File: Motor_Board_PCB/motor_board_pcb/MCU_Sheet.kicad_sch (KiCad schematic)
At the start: 63 parts, among them J1 CX90B-16P, J2 Barrel_Jack_Switch, J3 TSM-105-01-S-DV-M-TR, J5 PH2-06-UA, SW2 SW_Push, U1 R7FA4M1AB3CFM, U2 AP63205WU-7, Y1 16MHz?

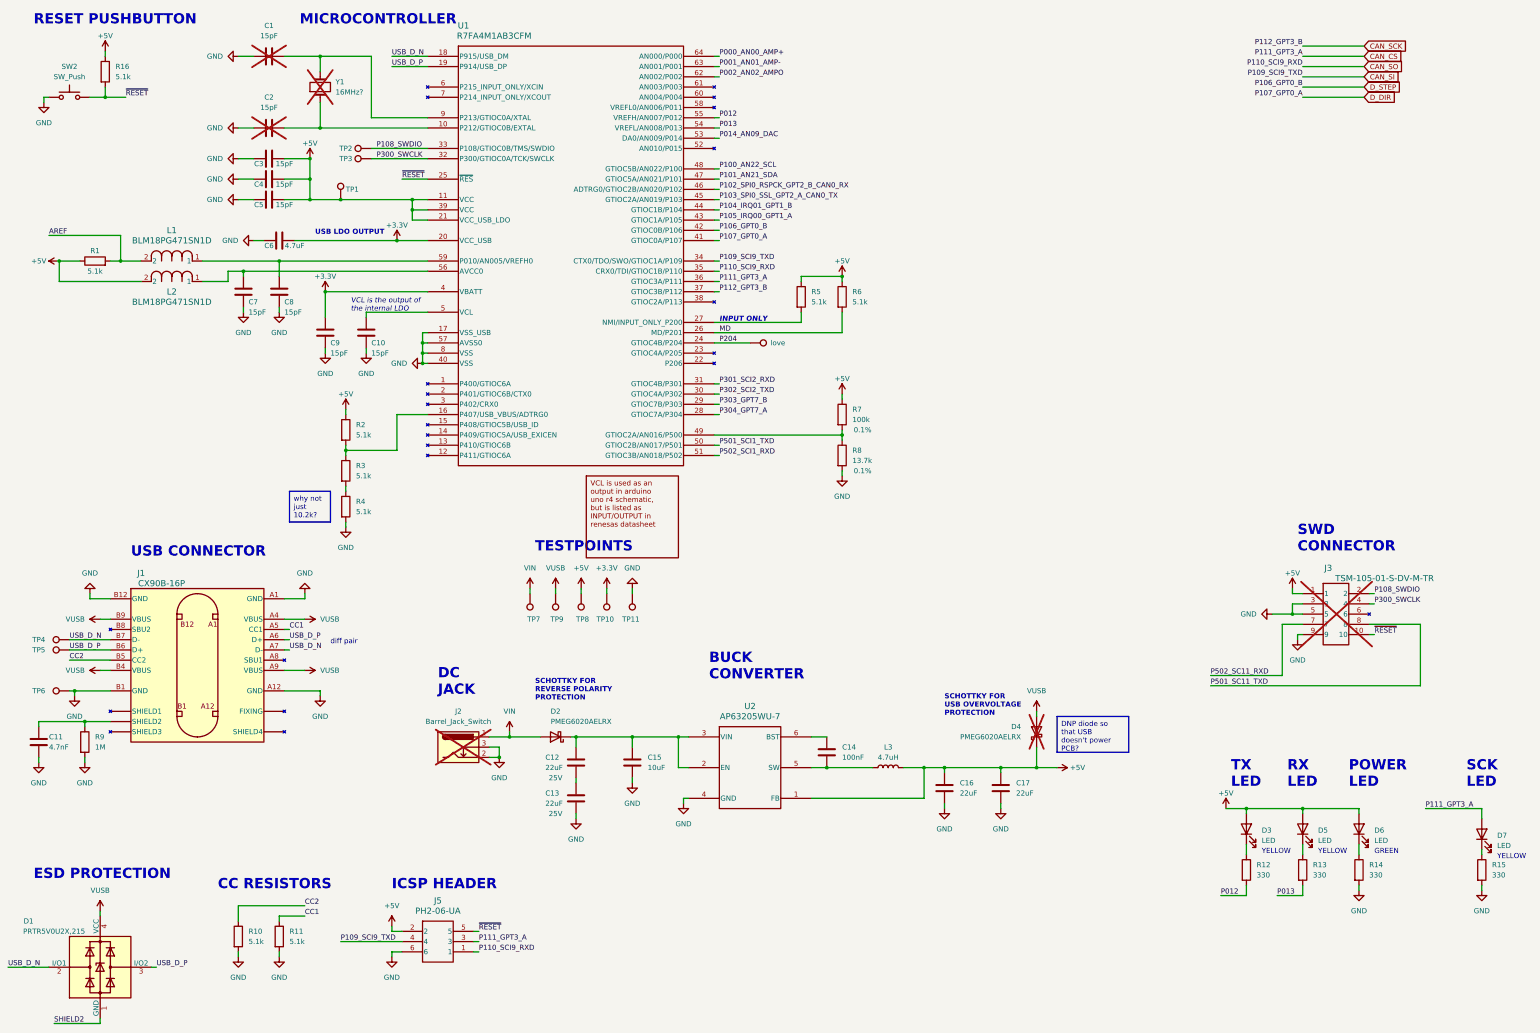
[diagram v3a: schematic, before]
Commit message: Added footprints for almost all components
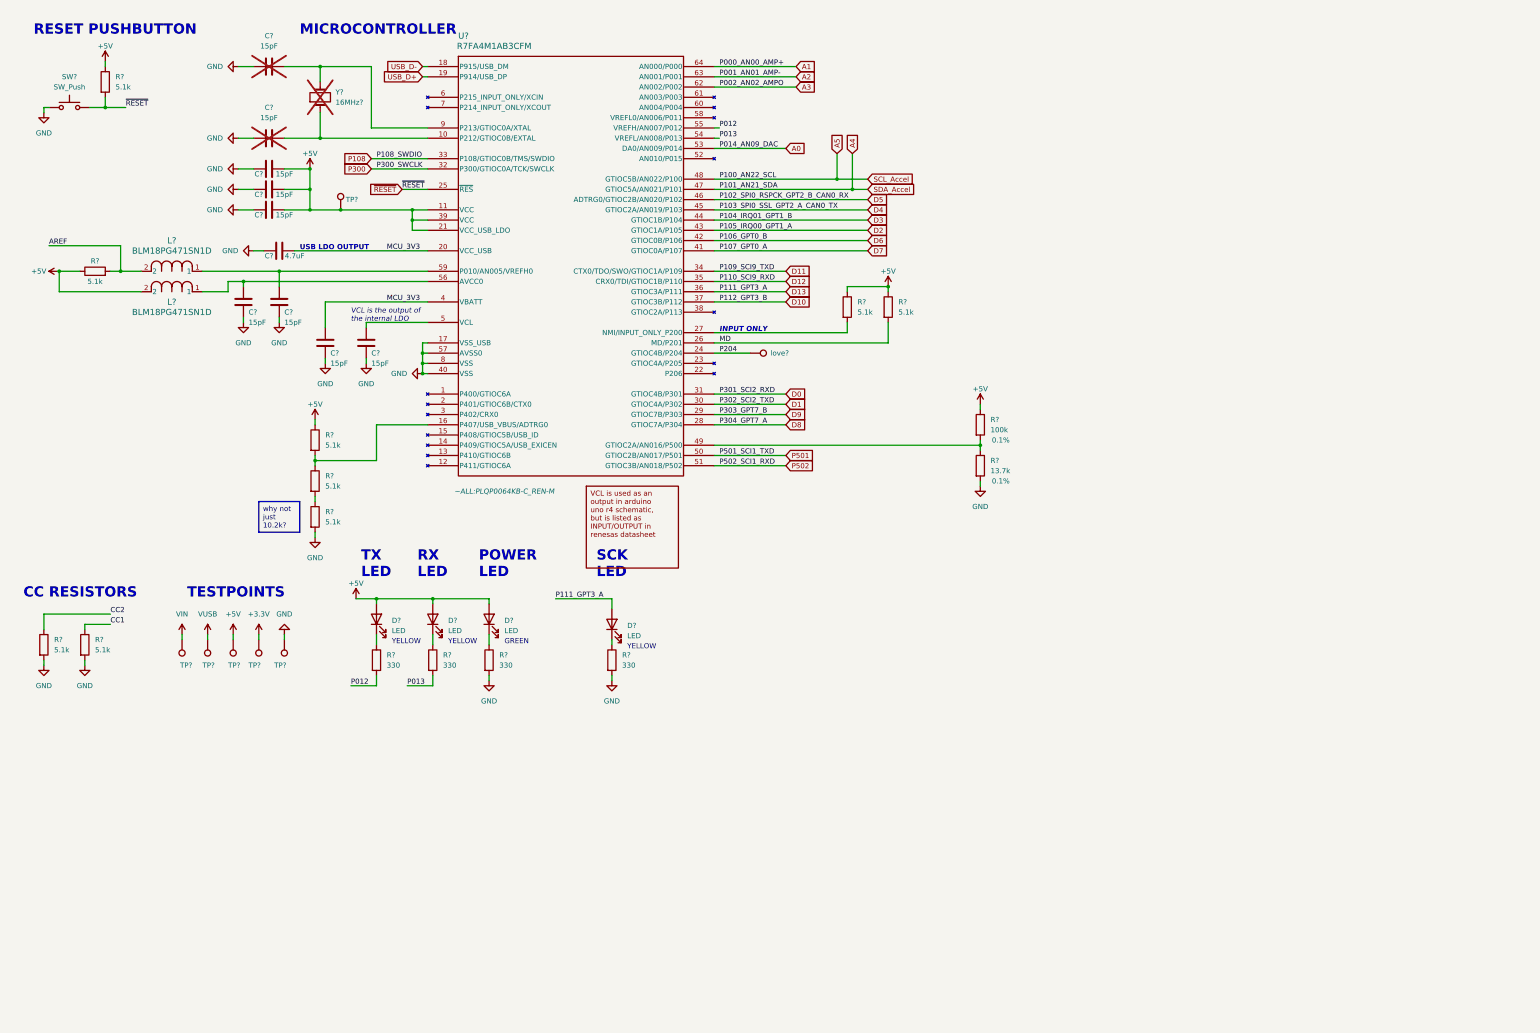
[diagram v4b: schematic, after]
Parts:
- removed C1, C10, C2, C3, C4, C5, C7, C8, C9: 15pF, symbol Device:C
- removed C11: 4.7nF, symbol Device:C
- removed C12, C13, C16, C17: 22uF, symbol Device:C
- removed C14: 100nF, symbol Device:C
- removed C15: 10uF, symbol Device:C
- removed C6: 4.7uF, symbol Device:C
- removed D1: PRTR5V0U2X,215, Package_TO_SOT_SMD:SOT-143, symbol Power_Protection:PRTR5V0U2X
- removed D2, D4: PMEG6020AELRX, Diode_SMD:Nexperia_CFP3_SOD-123W, symbol Diode:PMEG6020AELR
- removed D3, D5, D6, D7: LED, symbol Device:LED
- removed J1: CX90B-16P, CON18_1X12_P0_HIR, symbol CX90B-16P:CX90B-16P
- removed J2: Barrel_Jack_Switch, symbol Connector:Barrel_Jack_Switch
- removed J3: TSM-105-01-S-DV-M-TR, CONN_TSM-105-01-S-DV-M-TR_SAI, symbol TSM-105-01-S-DV-M-TR:TSM-105-01-S-DV-M-TR
- removed J5: PH2-06-UA, CONN_PH2-06-UA_ADM, symbol PH2-06-UA:PH2-06-UA
- removed L1, L2: BLM18PG471SN1D, IND_BLM18_0603_MUR, symbol BLM18PG471SN1D:BLM18PG471SN1D
- removed L3: 4.7uH, symbol Device:L
- removed R1, R10, R11, R16, R2, R3, R4, R5, R6: 5.1k, symbol Device:R
- removed R12, R13, R14, R15: 330, symbol Device:R
- removed R7: 100k, symbol Device:R
- removed R8: 13.7k, symbol Device:R
- removed R9: 1M, symbol Device:R
- removed SW2: SW_Push, symbol Switch:SW_Push
- removed TP1, TP10, TP11, TP2, TP3, TP4, TP5, TP6, TP7, TP8, TP9, love: TestPoint, symbol Connector:TestPoint
- removed U1: R7FA4M1AB3CFM, PLQP0064KB-C_REN, symbol R7FA4M1AB3CFM:R7FA4M1AB3CFM
- removed U2: AP63205WU-7, SOIC_05WU-7_DIO, symbol AP63205WU-7:AP63205WU-7
- removed Y1: 16MHz?, symbol Device:Crystal
- added C? (x9): 15pF, Capacitor_SMD:C_0603_1608Metric, symbol Device:C
- added C?: 4.7uF, Capacitor_SMD:C_0603_1608Metric, symbol Device:C
- added D? (x4): LED, Diode_SMD:D_0603_1608Metric, symbol Device:LED
- added L? (x2): BLM18PG471SN1D, ~ALL:IND_BLM18_0603_MUR, symbol BLM18PG471SN1D:BLM18PG471SN1D
- added R? (x4): 330, Resistor_SMD:R_0603_1608Metric, symbol Device:R
- added R? (x9): 5.1k, Resistor_SMD:R_0603_1608Metric, symbol Device:R
- added R?: 13.7k, Resistor_SMD:R_0603_1608Metric, symbol Device:R
- added R?: 100k, Resistor_SMD:R_0603_1608Metric, symbol Device:R
- added SW?: SW_Push, Button_Switch_SMD:SW_Push_1P1T_NO_6x6mm_H9.5mm, symbol Switch:SW_Push
- added TP? (x6): TestPoint, TestPoint:TestPoint_Pad_D1.0mm, symbol Connector:TestPoint
- added U?: R7FA4M1AB3CFM, ~ALL:PLQP0064KB-C_REN-M, symbol R7FA4M1AB3CFM:R7FA4M1AB3CFM
- added Y?: 16MHz?, symbol Device:Crystal
- added love?: TestPoint, TestPoint:TestPoint_Pad_D2.0mm, symbol Connector:TestPoint
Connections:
- net +3.3V: now also TP?.1
- net +5V: now also C?.2, C?.2, C?.2, D?.2 (A), D?.2 (A), D?.2 (A), L?.2, R?.1, R?.1, R?.1, R?.1, R?.1, R?.1, TP?.1, TP?.1, U?.11 (VCC), U?.21 (VCC_USB_LDO), U?.39 (VCC)
- net AREF: now also L?.2, R?.2
- net CC1: now also R?.1
- net CC2: now also R?.1
- net GND: now also C?.1, C?.1, C?.1, C?.1, C?.1, C?.1, C?.1, C?.1, C?.1, C?.1, R?.2, R?.2, R?.2, R?.2, R?.2, R?.2, SW?.1, TP?.1, U?.17 (VSS_USB), U?.40 (VSS), U?.57 (AVSS0), U?.8 (VSS)
- net MD: now also R?.2, U?.26 (MD/P201)
- net P012: now also R?.2, U?.55 (VREFH/AN007/P012)
- net P013: now also R?.2, U?.54 (VREFL/AN008/P013)
- net P204: now also U?.24 (GTIOC4B/P204), love?.1
- net VUSB: now also TP?.1, TP?.1
- net ~{RESET}: now also R?.2, SW?.2, U?.25 (~{RES})
- new net: D?.1 (K), R?.1 (x4)
- new net: C?.2, U?.9 (P213/GTIOC0A/XTAL), Y?.2
- new net: C?.2, L?.1, U?.59 (P010/AN005/VREFH0)
- new net: R?.1, R?.2, U?.16 (P407/USB_VBUS/ADTRG0)
- new net: R?.1, R?.2
- new net: C?.2, U?.10 (P212/GTIOC0B/EXTAL), Y?.1
- new net: R?.2, U?.27 (NMI/INPUT_ONLY_P200)
- new net: R?.1, R?.2, U?.49 (GTIOC2A/AN016/P500)
- new net: C?.2, U?.5 (VCL)
- new net: C?.2, L?.1, U?.56 (AVCC0)
- new net A0: U?.53 (DA0/AN009/P014)
- new net A1: U?.64 (AN000/P000)
- new net A2: U?.63 (AN001/P001)
- new net A3: U?.62 (AN002/P002)
- new net A4: U?.47 (GTIOC5A/AN021/P101)
- new net A5: U?.48 (GTIOC5B/AN022/P100)
- new net D0: U?.31 (GTIOC4B/P301)
- new net D1: U?.30 (GTIOC4A/P302)
- new net D10: U?.37 (GTIOC3B/P112)
- new net D11: U?.34 (CTX0/TDO/SWO/GTIOC1A/P109)
- new net D12: U?.35 (CRX0/TDI/GTIOC1B/P110)
- new net D13: D?.2 (A), U?.36 (GTIOC3A/P111)
- new net D2: U?.43 (GTIOC1A/P105)
- new net D3: U?.44 (GTIOC1B/P104)
- new net D4: U?.45 (GTIOC2A/AN019/P103)
- new net D5: U?.46 (ADTRG0/GTIOC2B/AN020/P102)
- new net D6: U?.42 (GTIOC0B/P106)
- new net D7: U?.41 (GTIOC0A/P107)
- new net D8: U?.28 (GTIOC7A/P304)
- new net D9: U?.29 (GTIOC7B/P303)
- new net MCU_3V3: C?.2, C?.2, U?.20 (VCC_USB), U?.4 (VBATT)
- new net P108: U?.33 (P108/GTIOC0B/TMS/SWDIO)
- new net P300: U?.32 (P300/GTIOC0A/TCK/SWCLK)
- new net P501: U?.50 (GTIOC2B/AN017/P501)
- new net P502: U?.51 (GTIOC3B/AN018/P502)
- new net USB_D+: U?.19 (P914/USB_DP)
- new net USB_D-: U?.18 (P915/USB_DM)
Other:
- note removed: "BUCK CONVERTER"
- note removed: "DC JACK"
- note removed: "ESD PROTECTION"
- note removed: "ICSP HEADER"
- note removed: "SCHOTTKY FOR REVERSE POLARITY PROTECTION"
- note removed: "SCHOTTKY FOR USB OVERVOLTAGE PROTECTION"
- note removed: "SWD CONNECTOR"
- note removed: "USB CONNECTOR"
- note removed: "diff pair"

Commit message: Added all other footprints... populated all components with NO errors or warnings :)
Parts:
- Y?: footprint (none) -> Crystal:Crystal_HC49-U_Vertical
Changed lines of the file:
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@@
       (effects (font (size 1.27 1.27)) (justify right))
     )
-    (property "Footprint" "" (at 92.71 41.91 0)
+    (property "Footprint" "Crystal:Crystal_HC49-U_Vertical" (at 92.71 41.91 0)
       (effects (font (size 1.27 1.27)) hide)
     )

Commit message: Meeting Changes
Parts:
- C? (x2), Y?: now fitted
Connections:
- net MD renamed BOOT
- net P108: no longer names the net of U?.33 (P108/GTIOC0B/TMS/SWDIO)
- net P300: no longer names the net of U?.32 (P300/GTIOC0A/TCK/SWCLK)
- net P501: no longer names the net of U?.50 (GTIOC2B/AN017/P501)
- net P502: no longer names the net of U?.51 (GTIOC3B/AN018/P502)
- no-connect marks 0 -> 4
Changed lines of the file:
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@@
   (junction (at 90.17 64.77) (diameter 0) (color 0 0 0 0)
   )
+  (junction (at 233.68 102.87) (diameter 0) (color 0 0 0 0)
+  )
   (junction (at 27.94 85.09) (diameter 0) (color 0 0 0 0)
   )
@@
   (junction (at 256.54 128.27) (diameter 0) (color 0 0 0 0)
   )
+  (no_connect (at 190.5 133.35))
+  (no_connect (at 119.38 59.69))
+  (no_connect (at 190.5 130.81))
+  (no_connect (at 119.38 57.15))
   (wire (pts (xy 190.5 54.61) (xy 208.28 54.61))
     (stroke (width 0) (type default))
@@
     (stroke (width 0) (type default))
   )
-  (wire (pts (xy 105.41 59.69) (xy 119.38 59.69))
-    (stroke (width 0) (type default))
-  )
   (wire (pts (xy 91.44 133.35) (xy 91.44 132.08))
     (stroke (width 0) (type default))
@@
     (stroke (width 0) (type default))
   )
-  (wire (pts (xy 190.5 133.35) (xy 208.28 133.35))
-    (stroke (width 0) (type default))
-  )
   (wire (pts (xy 40.64 85.09) (xy 43.18 85.09))
     (stroke (width 0) (type default))
@@
     (stroke (width 0) (type default))
   )
-  (wire (pts (xy 190.5 130.81) (xy 208.28 130.81))
-    (stroke (width 0) (type default))
-  )
   (wire (pts (xy 90.17 64.77) (xy 90.17 69.85))
     (stroke (width 0) (type default))
@@
     (stroke (width 0) (type default))
   )
+  (wire (pts (xy 233.68 102.87) (xy 237.49 102.87))
+    (stroke (width 0) (type default))
+  )
   (wire (pts (xy 190.5 128.27) (xy 256.54 128.27))
     (stroke (width 0) (type default))
@@
   )
   (wire (pts (xy 73.66 96.52) (xy 73.66 97.79))
-    (stroke (width 0) (type default))
-  )
-  (wire (pts (xy 105.41 57.15) (xy 119.38 57.15))
     (stroke (width 0) (type default))
   )
@@
     (effects (font (size 1.27 1.27)) (justify left bottom))
   )
-  (label "P502_SCI1_RXD" (at 191.77 133.35 0) (fields_autoplaced)
-    (effects (font (size 1.27 1.27)) (justify left bottom))
-  )
-  (label "CC1" (at 40.64 172.72 0) (fields_autoplaced)
-    (effects (font (size 1.27 1.27)) (justify left bottom))
-  )
   (label "~{RESET}" (at 113.03 64.77 0) (fields_autoplaced)
     (effects (font (size 1.27 1.27)) (justify left bottom))
@@
     (effects (font (size 1.27 1.27)) (justify left bottom))
   )
-  (label "P108_SWDIO" (at 106.68 57.15 0) (fields_autoplaced)
-    (effects (font (size 1.27 1.27)) (justify left bottom))
-  )
   (label "MD" (at 191.77 102.87 0) (fields_autoplaced)
     (effects (font (size 1.27 1.27)) (justify left bottom))
@@
     (effects (font (size 1.27 1.27)) (justify left bottom))
   )
-  (label "P501_SCI1_TXD" (at 191.77 130.81 0) (fields_autoplaced)
-    (effects (font (size 1.27 1.27)) (justify left bottom))
-  )
   (label "P110_SCI9_RXD" (at 191.77 87.63 0) (fields_autoplaced)
     (effects (font (size 1.27 1.27)) (justify left bottom))
@@
     (effects (font (size 1.27 1.27)) (justify left bottom))
   )
-  (label "CC2" (at 40.64 170.18 0) (fields_autoplaced)
-    (effects (font (size 1.27 1.27)) (justify left bottom))
-  )
   (label "P001_AN01_AMP-" (at 191.77 36.83 0) (fields_autoplaced)
     (effects (font (size 1.27 1.27)) (justify left bottom))
@@
     (effects (font (size 1.27 1.27)) (justify left bottom))
   )
-  (label "P300_SWCLK" (at 106.68 59.69 0) (fields_autoplaced)
-    (effects (font (size 1.27 1.27)) (justify left bottom))
+  (global_label "CC1" (shape input) (at 40.64 172.72 0) (fields_autoplaced)
+    (effects (font (size 1.27 1.27)) (justify left))
+    (property "Intersheetrefs" "${INTERSHEET_REFS}" (at 47.3747 172.72 0)
+      (effects (font (size 1.27 1.27)) (justify left) hide)
+    )
   )
   (global_label "USB_D+" (shape input) (at 118.11 36.83 180) (fields_autoplaced)
@@
     )
   )
+  (global_label "BOOT" (shape input) (at 237.49 102.87 0) (fields_autoplaced)
+    (effects (font (size 1.27 1.27)) (justify left))
+    (property "Intersheetrefs" "${INTERSHEET_REFS}" (at 245.3738 102.87 0)
+      (effects (font (size 1.27 1.27)) (justify left) hide)
+    )
+  )
   (global_label "SDA_Accel" (shape input) (at 228.6 64.77 0) (fields_autoplaced)
     (effects (font (size 1.27 1.27)) (justify left))
@@
     (property "Intersheetrefs" "${INTERSHEET_REFS}" (at 216.1033 36.83 0)
       (effects (font (size 1.27 1.27)) (justify left) hide)
-    )
-  )
-  (global_label "P108" (shape input) (at 105.41 57.15 180) (fields_autoplaced)
-    (effects (font (size 1.27 1.27)) (justify right))
-    (property "Intersheetrefs" "${INTERSHEET_REFS}" (at 97.5263 57.15 0)
-      (effects (font (size 1.27 1.27)) (justify right) hide)
     )
   )
@@
     )
   )
+  (global_label "CC2" (shape input) (at 40.64 170.18 0) (fields_autoplaced)
+    (effects (font (size 1.27 1.27)) (justify left))
+    (property "Intersheetrefs" "${INTERSHEET_REFS}" (at 47.3747 170.18 0)
+      (effects (font (size 1.27 1.27)) (justify left) hide)
+    )
+  )
   (global_label "D3" (shape input) (at 228.6 72.39 0) (fields_autoplaced)
     (effects (font (size 1.27 1.27)) (justify left))
@@
     )
   )
-  (global_label "P501" (shape input) (at 208.28 130.81 0) (fields_autoplaced)
-    (effects (font (size 1.27 1.27)) (justify left))
-    (property "Intersheetrefs" "${INTERSHEET_REFS}" (at 216.1637 130.81 0)
-      (effects (font (size 1.27 1.27)) (justify left) hide)
-    )
-  )
   (global_label "D1" (shape input) (at 208.28 118.11 0) (fields_autoplaced)
     (effects (font (size 1.27 1.27)) (justify left))
@@
     )
   )
-  (global_label "P300" (shape input) (at 105.41 59.69 180) (fields_autoplaced)
-    (effects (font (size 1.27 1.27)) (justify right))
-    (property "Intersheetrefs" "${INTERSHEET_REFS}" (at 97.5263 59.69 0)
-      (effects (font (size 1.27 1.27)) (justify right) hide)
-    )
-  )
   (global_label "A3" (shape input) (at 210.82 39.37 0) (fields_autoplaced)
     (effects (font (size 1.27 1.27)) (justify left))
@@
     (effects (font (size 1.27 1.27)) (justify left))
     (property "Intersheetrefs" "${INTERSHEET_REFS}" (at 216.1033 34.29 0)
-      (effects (font (size 1.27 1.27)) (justify left) hide)
-    )
-  )
-  (global_label "P502" (shape input) (at 208.28 133.35 0) (fields_autoplaced)
-    (effects (font (size 1.27 1.27)) (justify left))
-    (property "Intersheetrefs" "${INTERSHEET_REFS}" (at 216.1637 133.35 0)
       (effects (font (size 1.27 1.27)) (justify left) hide)
     )
@@
   )
   (symbol (lib_id "Device:C") (at 80.01 34.29 90) (unit 1)
-    (in_bom yes) (on_board yes) (dnp yes) (fields_autoplaced)
+    (in_bom yes) (on_board yes) (dnp no) (fields_autoplaced)
     (property "Reference" "C?" (at 80.01 26.67 90)
       (effects (font (size 1.27 1.27)))
@@
   )
   (symbol (lib_id "Device:Crystal") (at 92.71 41.91 90) (unit 1)
-    (in_bom yes) (on_board yes) (dnp yes) (fields_autoplaced)
+    (in_bom yes) (on_board yes) (dnp no) (fields_autoplaced)
     (property "Reference" "Y?" (at 96.52 40.64 90)
       (effects (font (size 1.27 1.27)) (justify right))
@@
   )
   (symbol (lib_id "Device:C") (at 80.01 52.07 90) (unit 1)
-    (in_bom yes) (on_board yes) (dnp yes) (fields_autoplaced)
+    (in_bom yes) (on_board yes) (dnp no) (fields_autoplaced)
     (property "Reference" "C?" (at 80.01 44.45 90)
       (effects (font (size 1.27 1.27)))

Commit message: - fixed capacitor values on MCU sheet (both central hub and motor board) - added missing Accelerometer componenets - changed BOOT HEADER (both central hub and motor board) - set the Arduino "love" signal to NC - fixed overlapping pins on USB connector
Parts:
- removed love?: TestPoint, TestPoint:TestPoint_Pad_D2.0mm, symbol Connector:TestPoint
- C? (x4): value 15pF -> 100nF
- C?: value 15pF -> 1uF
- C? (x2): value 15pF -> 4.7uF
- U?: footprint ~ALL:PLQP0064KB-C_REN-M -> PLQP0064KB-C_REN
- Y?: value 16MHz? -> 16MHz
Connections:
- net P204: no longer names the net of U?.24 (GTIOC4B/P204)
- no-connect marks 4 -> 5
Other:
- moved on the sheet: R?
